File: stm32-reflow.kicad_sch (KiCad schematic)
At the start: 7 parts

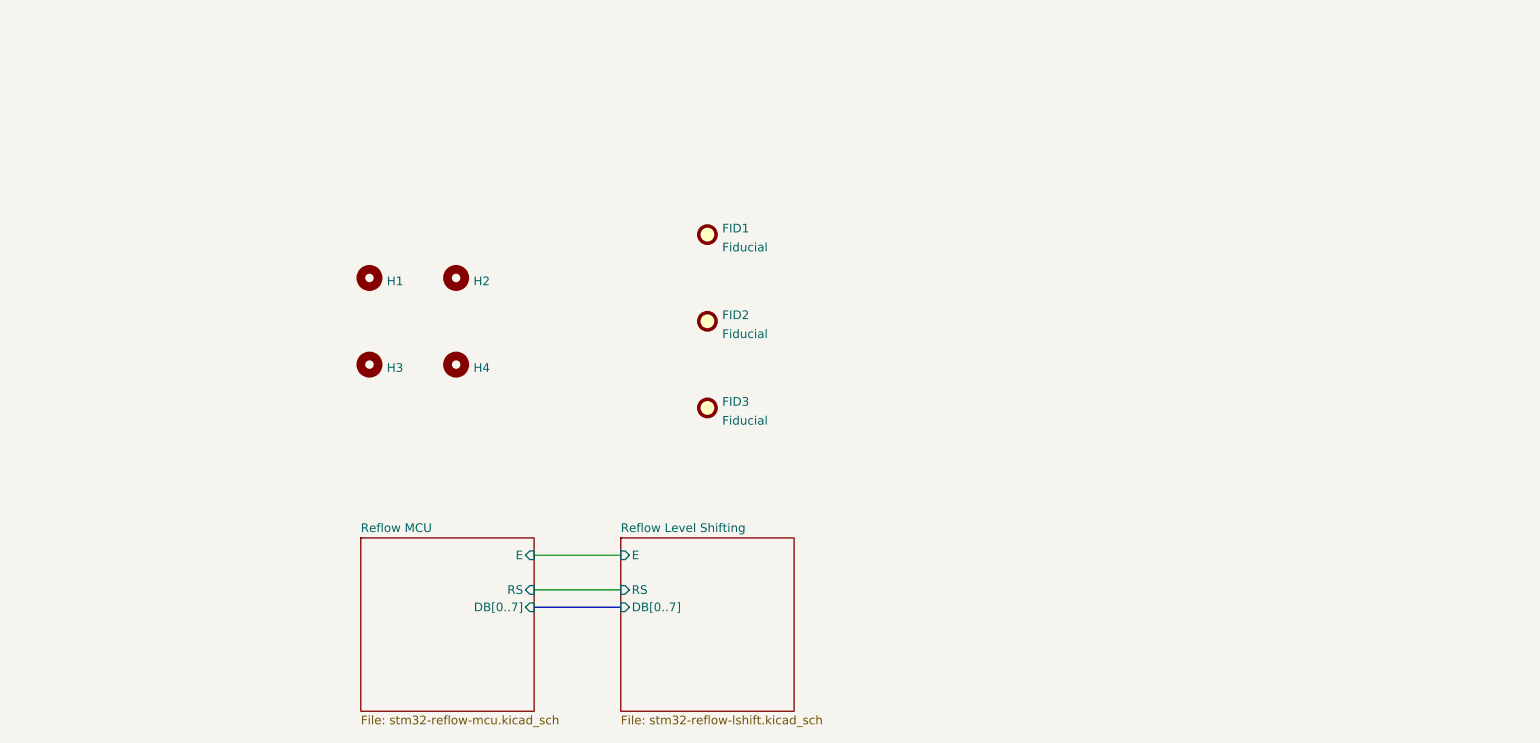
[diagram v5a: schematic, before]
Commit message: organized schematic more, fixed net naming of rw
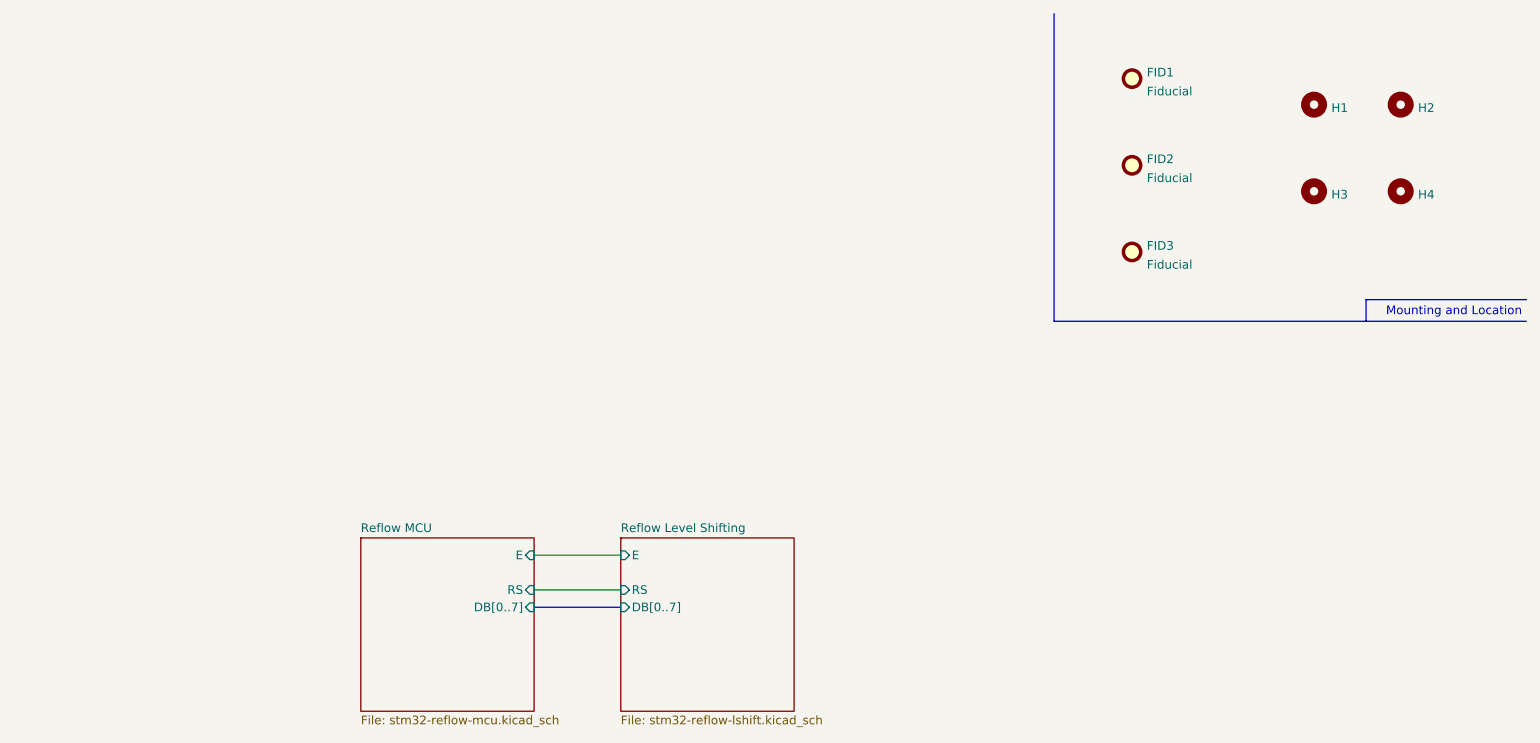
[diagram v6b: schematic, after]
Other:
- note added: "Mounting and Location"
- moved on the sheet: FID1, FID2, FID3, H1, H2, H3, H4
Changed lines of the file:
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@@
     (stroke (width 0) (type default) (color 0 0 0 0))
   )
-  (symbol (lib_id "Mechanical:Fiducial") (at 165.1 44.45 0) (unit 1)
-    (in_bom yes) (on_board yes) (fields_autoplaced)
-    (property "Reference" "FID1" (id 0) (at 167.259 43.5415 0)
-      (effects (font (size 1.27 1.27)) (justify left))
-    )
-    (property "Value" "Fiducial" (id 1) (at 167.259 46.3166 0)
-      (effects (font (size 1.27 1.27)) (justify left))
-    )
-    (property "Footprint" "Fiducial:Fiducial_0.75mm_Mask2.25mm" (id 2) (at 165.1 44.45 0)
-      (effects (font (size 1.27 1.27)) hide)
-    )
-    (property "Datasheet" "~" (id 3) (at 165.1 44.45 0)
-      (effects (font (size 1.27 1.27)) hide)
-    )
-  )
-  (symbol (lib_id "Mechanical:Fiducial") (at 165.1 57.15 0) (unit 1)
-    (in_bom yes) (on_board yes) (fields_autoplaced)
-    (property "Reference" "FID2" (id 0) (at 167.259 56.2415 0)
-      (effects (font (size 1.27 1.27)) (justify left))
-    )
-    (property "Value" "Fiducial" (id 1) (at 167.259 59.0166 0)
-      (effects (font (size 1.27 1.27)) (justify left))
-    )
-    (property "Footprint" "Fiducial:Fiducial_0.75mm_Mask2.25mm" (id 2) (at 165.1 57.15 0)
-      (effects (font (size 1.27 1.27)) hide)
-    )
-    (property "Datasheet" "~" (id 3) (at 165.1 57.15 0)
-      (effects (font (size 1.27 1.27)) hide)
-    )
-  )
-  (symbol (lib_id "Mechanical:Fiducial") (at 165.1 69.85 0) (unit 1)
-    (in_bom yes) (on_board yes) (fields_autoplaced)
-    (property "Reference" "FID3" (id 0) (at 167.259 68.9415 0)
-      (effects (font (size 1.27 1.27)) (justify left))
-    )
-    (property "Value" "Fiducial" (id 1) (at 167.259 71.7166 0)
-      (effects (font (size 1.27 1.27)) (justify left))
-    )
-    (property "Footprint" "Fiducial:Fiducial_0.75mm_Mask2.25mm" (id 2) (at 165.1 69.85 0)
-      (effects (font (size 1.27 1.27)) hide)
-    )
-    (property "Datasheet" "~" (id 3) (at 165.1 69.85 0)
-      (effects (font (size 1.27 1.27)) hide)
-    )
-  )
-  (symbol (lib_id "Mechanical:MountingHole") (at 115.57 50.8 0) (unit 1)
-    (in_bom yes) (on_board yes) (fields_autoplaced)
-    (property "Reference" "H1" (id 0) (at 118.11 51.279 0)
-      (effects (font (size 1.27 1.27)) (justify left))
-    )
-    (property "Value" "MountingHole" (id 1) (at 118.11 52.6666 0)
+  (polyline (pts (xy 215.9 12.065) (xy 215.9 57.15))
+    (stroke (width 0) (type default) (color 0 0 0 0))
+  )
+  (polyline (pts (xy 215.9 57.15) (xy 285.115 57.15))
+    (stroke (width 0) (type default) (color 0 0 0 0))
+  )
+  (polyline (pts (xy 261.62 53.975) (xy 261.62 57.15))
+    (stroke (width 0) (type default) (color 0 0 0 0))
+  )
+  (polyline (pts (xy 285.115 53.975) (xy 261.62 53.975))
+    (stroke (width 0) (type default) (color 0 0 0 0))
+  )
+  (text "Mounting and Location" (at 284.48 56.515 180)
+    (effects (font (size 1.27 1.27)) (justify right bottom))
+  )
+  (symbol (lib_id "Mechanical:Fiducial") (at 227.33 21.59 0) (unit 1)
+    (in_bom yes) (on_board yes) (fields_autoplaced)
+    (property "Reference" "FID1" (id 0) (at 229.489 20.6815 0)
+      (effects (font (size 1.27 1.27)) (justify left))
+    )
+    (property "Value" "Fiducial" (id 1) (at 229.489 23.4566 0)
+      (effects (font (size 1.27 1.27)) (justify left))
+    )
+    (property "Footprint" "Fiducial:Fiducial_0.75mm_Mask2.25mm" (id 2) (at 227.33 21.59 0)
+      (effects (font (size 1.27 1.27)) hide)
+    )
+    (property "Datasheet" "~" (id 3) (at 227.33 21.59 0)
+      (effects (font (size 1.27 1.27)) hide)
+    )
+  )
+  (symbol (lib_id "Mechanical:Fiducial") (at 227.33 34.29 0) (unit 1)
+    (in_bom yes) (on_board yes) (fields_autoplaced)
+    (property "Reference" "FID2" (id 0) (at 229.489 33.3815 0)
+      (effects (font (size 1.27 1.27)) (justify left))
+    )
+    (property "Value" "Fiducial" (id 1) (at 229.489 36.1566 0)
+      (effects (font (size 1.27 1.27)) (justify left))
+    )
+    (property "Footprint" "Fiducial:Fiducial_0.75mm_Mask2.25mm" (id 2) (at 227.33 34.29 0)
+      (effects (font (size 1.27 1.27)) hide)
+    )
+    (property "Datasheet" "~" (id 3) (at 227.33 34.29 0)
+      (effects (font (size 1.27 1.27)) hide)
+    )
+  )
+  (symbol (lib_id "Mechanical:Fiducial") (at 227.33 46.99 0) (unit 1)
+    (in_bom yes) (on_board yes) (fields_autoplaced)
+    (property "Reference" "FID3" (id 0) (at 229.489 46.0815 0)
+      (effects (font (size 1.27 1.27)) (justify left))
+    )
+    (property "Value" "Fiducial" (id 1) (at 229.489 48.8566 0)
+      (effects (font (size 1.27 1.27)) (justify left))
+    )
+    (property "Footprint" "Fiducial:Fiducial_0.75mm_Mask2.25mm" (id 2) (at 227.33 46.99 0)
+      (effects (font (size 1.27 1.27)) hide)
+    )
+    (property "Datasheet" "~" (id 3) (at 227.33 46.99 0)
+      (effects (font (size 1.27 1.27)) hide)
+    )
+  )
+  (symbol (lib_id "Mechanical:MountingHole") (at 254 25.4 0) (unit 1)
+    (in_bom yes) (on_board yes) (fields_autoplaced)
+    (property "Reference" "H1" (id 0) (at 256.54 25.879 0)
+      (effects (font (size 1.27 1.27)) (justify left))
+    )
+    (property "Value" "MountingHole" (id 1) (at 256.54 27.2666 0)
       (effects (font (size 1.27 1.27)) (justify left) hide)
     )
-    (property "Footprint" "MountingHole:MountingHole_2.7mm_M2.5_Pad_Via" (id 2) (at 115.57 50.8 0)
-      (effects (font (size 1.27 1.27)) hide)
-    )
-    (property "Datasheet" "~" (id 3) (at 115.57 50.8 0)
-      (effects (font (size 1.27 1.27)) hide)
-    )
-  )
-  (symbol (lib_id "Mechanical:MountingHole") (at 115.57 63.5 0) (unit 1)
-    (in_bom yes) (on_board yes) (fields_autoplaced)
-    (property "Reference" "H3" (id 0) (at 118.11 63.979 0)
-      (effects (font (size 1.27 1.27)) (justify left))
-    )
-    (property "Value" "MountingHole" (id 1) (at 118.11 65.3666 0)
+    (property "Footprint" "MountingHole:MountingHole_2.7mm_M2.5_Pad_Via" (id 2) (at 254 25.4 0)
+      (effects (font (size 1.27 1.27)) hide)
+    )
+    (property "Datasheet" "~" (id 3) (at 254 25.4 0)
+      (effects (font (size 1.27 1.27)) hide)
+    )
+  )
+  (symbol (lib_id "Mechanical:MountingHole") (at 254 38.1 0) (unit 1)
+    (in_bom yes) (on_board yes) (fields_autoplaced)
+    (property "Reference" "H3" (id 0) (at 256.54 38.579 0)
+      (effects (font (size 1.27 1.27)) (justify left))
+    )
+    (property "Value" "MountingHole" (id 1) (at 256.54 39.9666 0)
       (effects (font (size 1.27 1.27)) (justify left) hide)
     )
-    (property "Footprint" "MountingHole:MountingHole_2.7mm_M2.5_Pad_Via" (id 2) (at 115.57 63.5 0)
-      (effects (font (size 1.27 1.27)) hide)
-    )
-    (property "Datasheet" "~" (id 3) (at 115.57 63.5 0)
-      (effects (font (size 1.27 1.27)) hide)
-    )
-  )
-  (symbol (lib_id "Mechanical:MountingHole") (at 128.27 50.8 0) (unit 1)
-    (in_bom yes) (on_board yes) (fields_autoplaced)
-    (property "Reference" "H2" (id 0) (at 130.81 51.279 0)
-      (effects (font (size 1.27 1.27)) (justify left))
-    )
-    (property "Value" "MountingHole" (id 1) (at 130.81 52.6666 0)
+    (property "Footprint" "MountingHole:MountingHole_2.7mm_M2.5_Pad_Via" (id 2) (at 254 38.1 0)
+      (effects (font (size 1.27 1.27)) hide)
+    )
+    (property "Datasheet" "~" (id 3) (at 254 38.1 0)
+      (effects (font (size 1.27 1.27)) hide)
+    )
+  )
+  (symbol (lib_id "Mechanical:MountingHole") (at 266.7 25.4 0) (unit 1)
+    (in_bom yes) (on_board yes) (fields_autoplaced)
+    (property "Reference" "H2" (id 0) (at 269.24 25.879 0)
+      (effects (font (size 1.27 1.27)) (justify left))
+    )
+    (property "Value" "MountingHole" (id 1) (at 269.24 27.2666 0)
       (effects (font (size 1.27 1.27)) (justify left) hide)
     )
-    (property "Footprint" "MountingHole:MountingHole_2.7mm_M2.5_Pad_Via" (id 2) (at 128.27 50.8 0)
-      (effects (font (size 1.27 1.27)) hide)
-    )
-    (property "Datasheet" "~" (id 3) (at 128.27 50.8 0)
-      (effects (font (size 1.27 1.27)) hide)
-    )
-  )
-  (symbol (lib_id "Mechanical:MountingHole") (at 128.27 63.5 0) (unit 1)
-    (in_bom yes) (on_board yes) (fields_autoplaced)
-    (property "Reference" "H4" (id 0) (at 130.81 63.979 0)
-      (effects (font (size 1.27 1.27)) (justify left))
-    )
-    (property "Value" "MountingHole" (id 1) (at 130.81 65.3666 0)
+    (property "Footprint" "MountingHole:MountingHole_2.7mm_M2.5_Pad_Via" (id 2) (at 266.7 25.4 0)
+      (effects (font (size 1.27 1.27)) hide)
+    )
+    (property "Datasheet" "~" (id 3) (at 266.7 25.4 0)
+      (effects (font (size 1.27 1.27)) hide)
+    )
+  )
+  (symbol (lib_id "Mechanical:MountingHole") (at 266.7 38.1 0) (unit 1)
+    (in_bom yes) (on_board yes) (fields_autoplaced)
+    (property "Reference" "H4" (id 0) (at 269.24 38.579 0)
+      (effects (font (size 1.27 1.27)) (justify left))
+    )
+    (property "Value" "MountingHole" (id 1) (at 269.24 39.9666 0)
       (effects (font (size 1.27 1.27)) (justify left) hide)
     )
-    (property "Footprint" "MountingHole:MountingHole_2.7mm_M2.5_Pad_Via" (id 2) (at 128.27 63.5 0)
-      (effects (font (size 1.27 1.27)) hide)
-    )
-    (property "Datasheet" "~" (id 3) (at 128.27 63.5 0)
+    (property "Footprint" "MountingHole:MountingHole_2.7mm_M2.5_Pad_Via" (id 2) (at 266.7 38.1 0)
+      (effects (font (size 1.27 1.27)) hide)
+    )
+    (property "Datasheet" "~" (id 3) (at 266.7 38.1 0)
       (effects (font (size 1.27 1.27)) hide)
     )
@@
       (reference "#PWR0102") (unit 1) (value "GND") (footprint "")
     )
+    (path "/bd08278b-4287-4daa-92d4-6c7e541ec8a9/b67a99c9-f234-480b-8906-8e77cedec9d5"
+      (reference "#PWR0103") (unit 1) (value "GND") (footprint "")
+    )
     (path "/de6e3de0-902c-42f6-a583-3abfdd023979/b3ceba2d-3a02-4774-b690-8e877b8014ae"
